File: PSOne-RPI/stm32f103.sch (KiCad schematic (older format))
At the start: 25 parts, among them J10 Controller-Port, J11 Controller-Port, J14 FAN1, J15 CN701, J16 CN702, SW1 PWR_BTN, SW2 CD_CLOSED, U5 ULN2003, U6 ULN2003, U7 STM32F103RBTx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

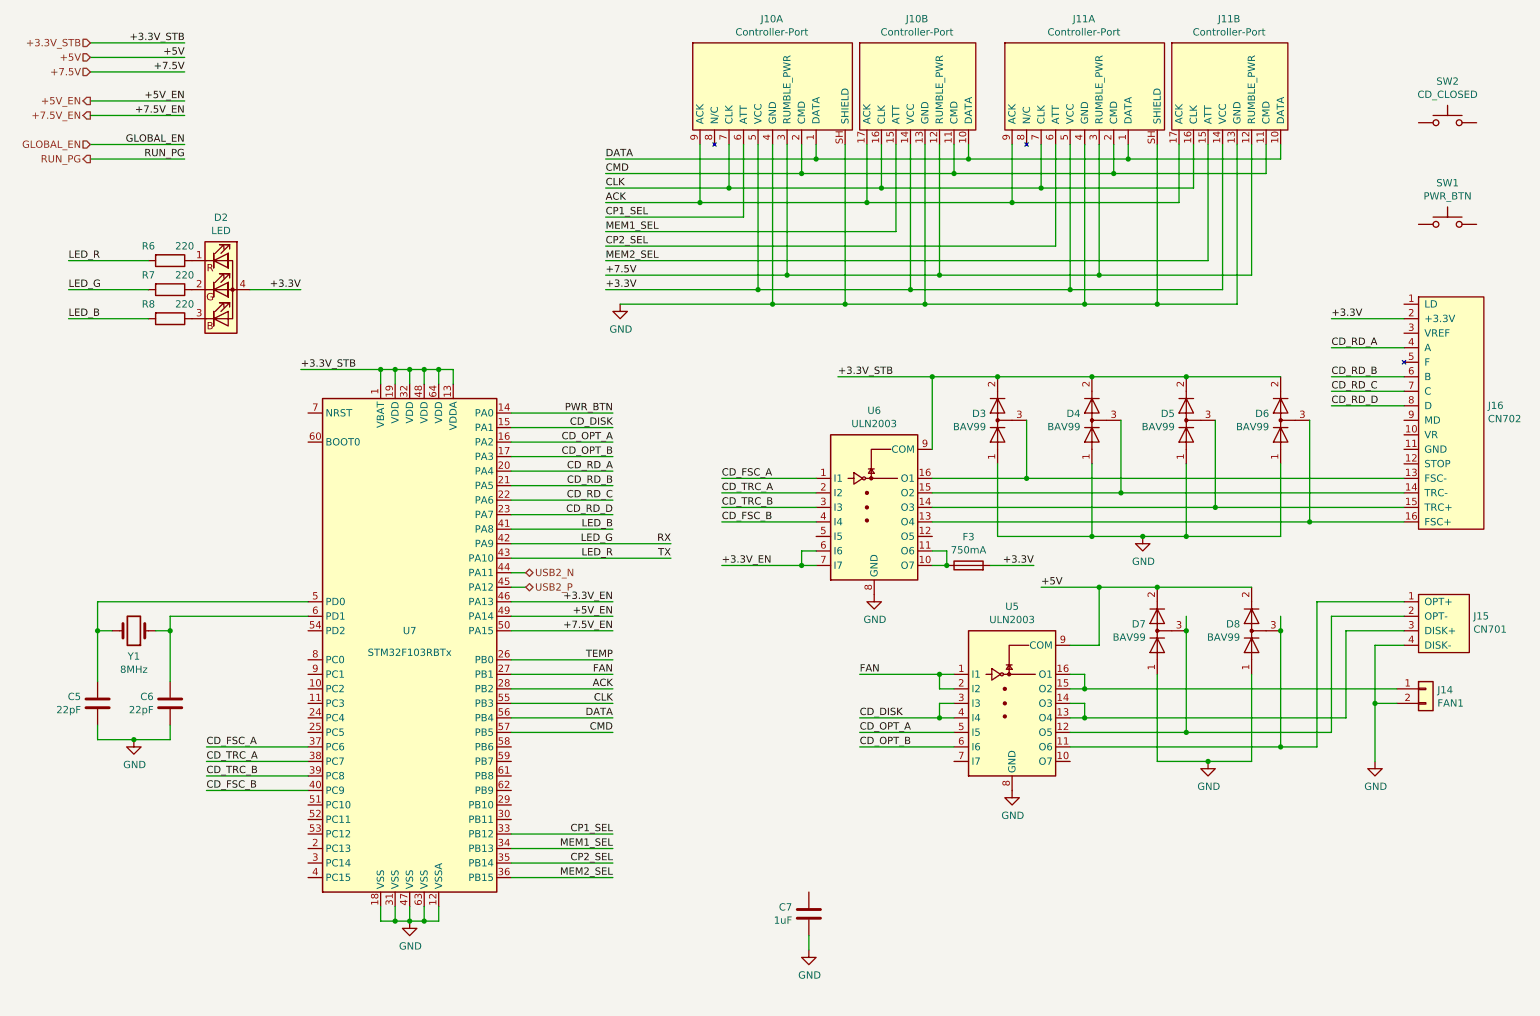
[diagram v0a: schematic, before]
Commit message: Cleaned schematic and moved CD interface to extra sheet
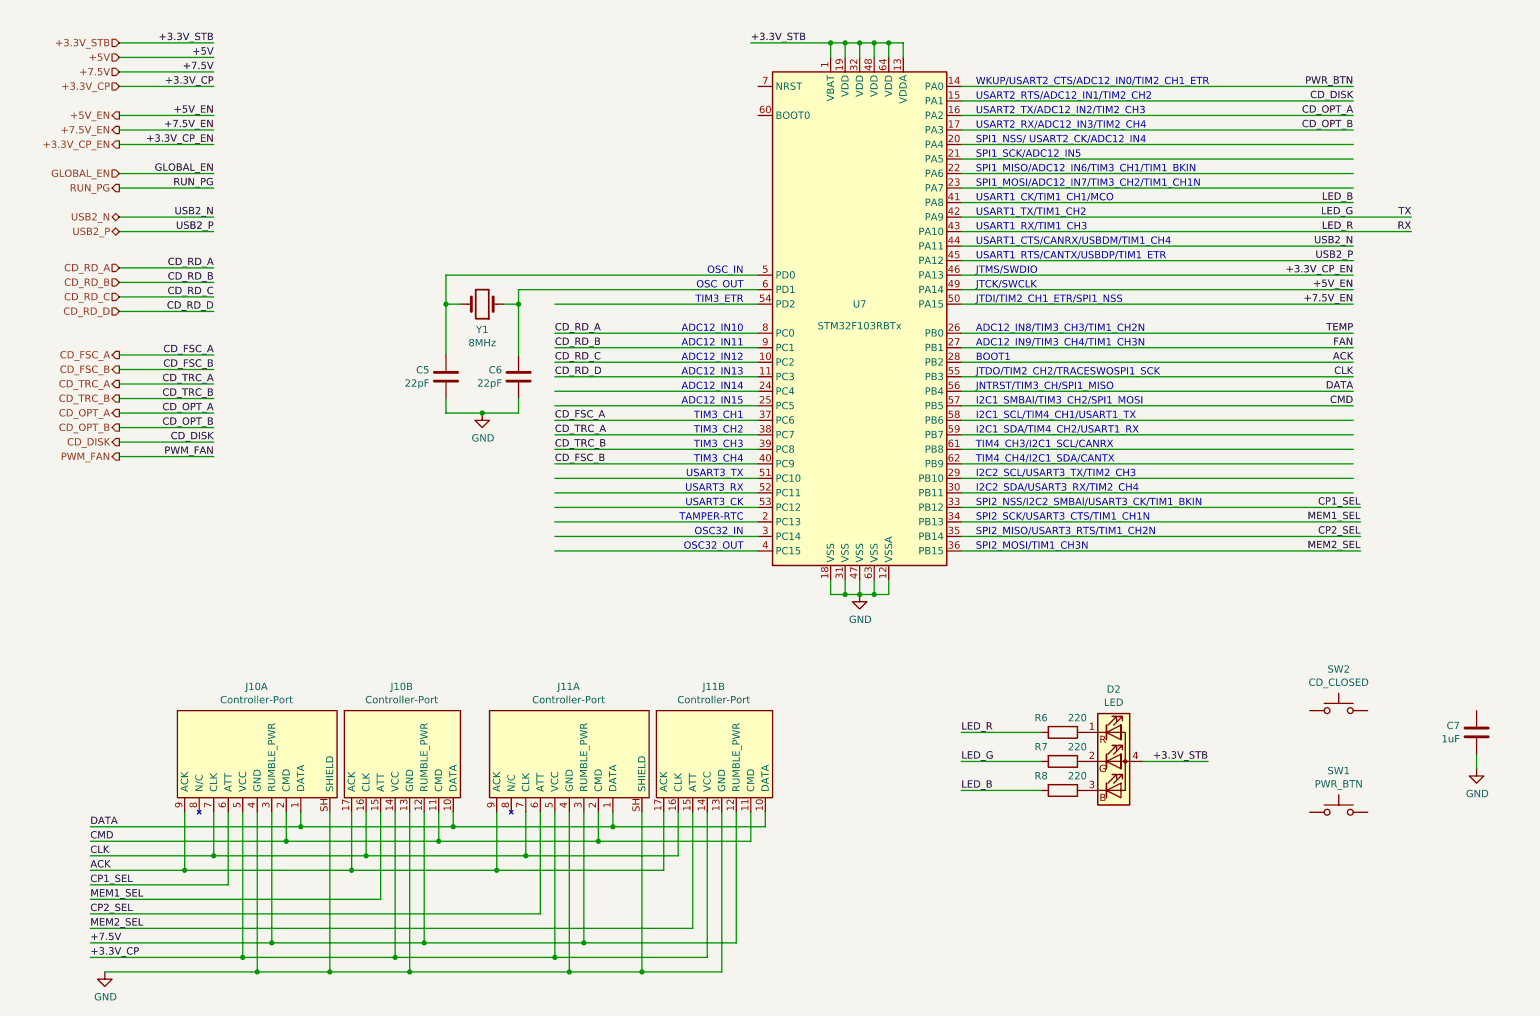
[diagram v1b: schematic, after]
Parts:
- removed D3, D4, D5, D6, D7, D8: BAV99, Package_TO_SOT_SMD:SOT-23, symbol Diode:BAV99
- removed F3: 750mA, Fuse:Fuse_1210_3225Metric, symbol Device:Fuse
- removed J14: FAN1, Connector_Hirose:Hirose_DF13-02P-1.25DSA_1x02_P1.25mm_Vertical, symbol Connector_Generic:Conn_01x02
- removed J15: CN701, Connector_Hirose:Hirose_DF13-04P-1.25DSA_1x04_P1.25mm_Vertical, symbol PSOne-RPI:CN701
- removed J16: CN702, PSOne-RPI:FFC-1x16-Vertical, symbol PSOne-RPI:CN702
- removed U5, U6: ULN2003, Package_SO:SOIC-16_3.9x9.9mm_P1.27mm, symbol Transistor_Array:ULN2003
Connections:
- net labels added: +3.3V_CP, +3.3V_CP_EN, PWM_FAN
- net labels removed: +3.3V, +3.3V_EN
- wire segments 231 -> 178
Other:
- note added: "ADC12_IN10"
- note added: "ADC12_IN11"
- note added: "ADC12_IN12"
- note added: "ADC12_IN13"
- note added: "ADC12_IN14"
- note added: "ADC12_IN15"
- note added: "ADC12_IN8/TIM3_CH3/TIM1_CH2N"
- note added: "ADC12_IN9/TIM3_CH4/TIM1_CH3N"
- note added: "BOOT1"
- note added: "I2C1_SCL/TIM4_CH1/USART1_TX"
- note added: "I2C1_SDA/TIM4_CH2/USART1_RX"
- note added: "I2C1_SMBAl/TIM3_CH2/SPI1_MOSI"
- note added: "I2C2_SCL/USART3_TX/TIM2_CH3"
- note added: "I2C2_SDA/USART3_RX/TIM2_CH4"
- note added: "JNTRST/TIM3_CH/SPI1_MISO"
- note added: "JTCK/SWCLK"
- note added: "JTDI/TIM2_CH1_ETR/SPI1_NSS"
- note added: "JTDO/TIM2_CH2/TRACESWOSPI1_SCK"
- note added: "JTMS/SWDIO"
- note added: "OSC32_IN"
- note added: "OSC32_OUT"
- note added: "OSC_IN"
- note added: "OSC_OUT"
- note added: "SPI1_MISO/ADC12_IN6/TIM3_CH1/TIM1_BKIN"
- note added: "SPI1_MOSI/ADC12_IN7/TIM3_CH2/TIM1_CH1N"
- note added: "SPI1_NSS/ USART2_CK/ADC12_IN4"
- note added: "SPI1_SCK/ADC12_IN5"
- note added: "SPI2_MISO/USART3_RTS/TIM1_CH2N"
- note added: "SPI2_MOSI/TIM1_CH3N"
- note added: "SPI2_NSS/I2C2_SMBAl/USART3_CK/TIM1_BKIN"
- note added: "SPI2_SCK/USART3_CTS/TIM1_CH1N"
- note added: "TAMPER-RTC"
- note added: "TIM3_CH1"
- note added: "TIM3_CH2"
- note added: "TIM3_CH3"
- note added: "TIM3_CH4"
- note added: "TIM3_ETR"
- note added: "TIM4_CH3/I2C1_SCL/CANRX"
- note added: "TIM4_CH4/I2C1_SDA/CANTX"
- note added: "USART1_CK/TIM1_CH1/MCO"
- note added: "USART1_CTS/CANRX/USBDM/TIM1_CH4"
- note added: "USART1_RTS/CANTX/USBDP/TIM1_ETR"
- note added: "USART1_RX/TIM1_CH3"
- note added: "USART1_TX/TIM1_CH2"
- note added: "USART2_RTS/ADC12_IN1/TIM2_CH2"
- note added: "USART2_RX/ADC12_IN3/TIM2_CH4"
- note added: "USART2_TX/ADC12_IN2/TIM2_CH3"
- note added: "USART3_CK"
- note added: "USART3_RX"
- note added: "USART3_TX"
- note added: "WKUP/USART2_CTS/ADC12_IN0/TIM2_CH1_ETR"
- moved on the sheet: C5, C6, C7, D2, J10A, J10B, J11A, J11B, R6, R7, R8, SW1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

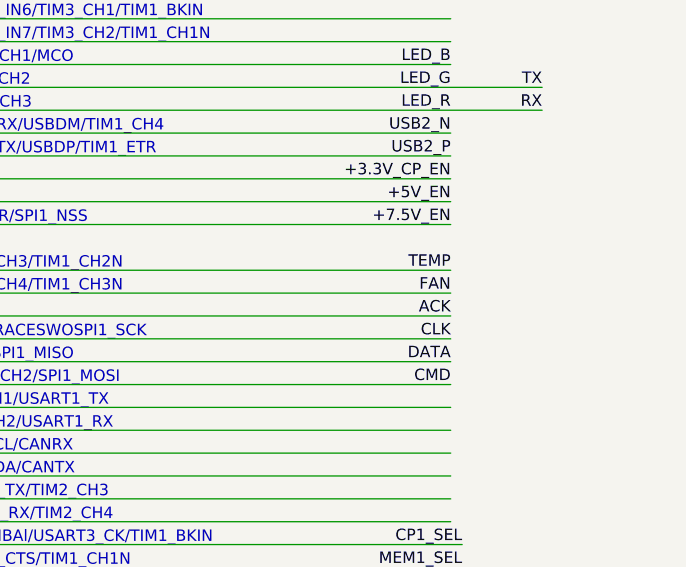
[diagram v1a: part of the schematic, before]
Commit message: Fixed naming FAN to PWM_FAN
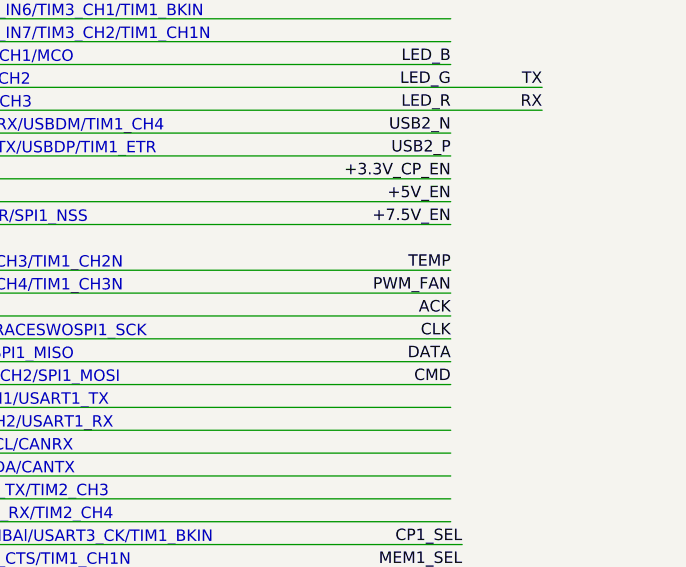
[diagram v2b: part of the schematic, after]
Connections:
- net labels removed: FAN
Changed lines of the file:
@@
 TEMP
 Text Label 9900 2950 2    50   ~ 0
-FAN
+PWM_FAN
 Text Label 9900 1450 2    50   ~ 0
 CD_OPT_B

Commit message: Finished CD drive interface circuit
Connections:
- net labels added: CD_LD, CD_MD, CD_STOP
- wire segments 178 -> 181
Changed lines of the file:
@@
 Text Label 2050 2700 2    50   ~ 0
 CD_RD_D
-Text HLabel 1400 3000 0    50   Output ~ 0
+Text HLabel 1400 2950 0    50   Output ~ 0
 CD_FSC_A
-Text HLabel 1400 3100 0    50   Output ~ 0
+Text HLabel 1400 3050 0    50   Output ~ 0
 CD_FSC_B
-Text HLabel 1400 3200 0    50   Output ~ 0
+Text HLabel 1400 3150 0    50   Output ~ 0
 CD_TRC_A
-Text HLabel 1400 3300 0    50   Output ~ 0
+Text HLabel 1400 3250 0    50   Output ~ 0
 CD_TRC_B
 Wire Wire Line
-	1400 3000 2050 3000
-Wire Wire Line
-	1400 3100 2050 3100
-Text Label 2050 3000 2    50   ~ 0
+	1400 2950 2050 2950
+Wire Wire Line
+	1400 3050 2050 3050
+Text Label 2050 2950 2    50   ~ 0
 CD_FSC_A
-Text Label 2050 3100 2    50   ~ 0
+Text Label 2050 3050 2    50   ~ 0
 CD_FSC_B
 Wire Wire Line
-	1400 3200 2050 3200
-Wire Wire Line
-	1400 3300 2050 3300
-Text Label 2050 3200 2    50   ~ 0
+	1400 3150 2050 3150
+Wire Wire Line
+	1400 3250 2050 3250
+Text Label 2050 3150 2    50   ~ 0
 CD_TRC_A
-Text Label 2050 3300 2    50   ~ 0
+Text Label 2050 3250 2    50   ~ 0
 CD_TRC_B
-Text HLabel 1400 3400 0    50   Output ~ 0
+Text HLabel 1400 3350 0    50   Output ~ 0
 CD_OPT_A
-Text HLabel 1400 3500 0    50   Output ~ 0
+Text HLabel 1400 3450 0    50   Output ~ 0
 CD_OPT_B
 Wire Wire Line
-	1400 3400 2050 3400
-Wire Wire Line
-	1400 3500 2050 3500
-Text Label 2050 3400 2    50   ~ 0
+	1400 3350 2050 3350
+Wire Wire Line
+	1400 3450 2050 3450
+Text Label 2050 3350 2    50   ~ 0
 CD_OPT_A
-Text Label 2050 3500 2    50   ~ 0
+Text Label 2050 3450 2    50   ~ 0
 CD_OPT_B
-Text HLabel 1400 3600 0    50   Output ~ 0
+Text HLabel 1400 3550 0    50   Output ~ 0
 CD_DISK
 Wire Wire Line
-	1400 3600 2050 3600
-Text Label 2050 3600 2    50   ~ 0
+	1400 3550 2050 3550
+Text Label 2050 3550 2    50   ~ 0
 CD_DISK
-Text HLabel 1400 3700 0    50   Output ~ 0
+Text HLabel 1400 4150 0    50   Output ~ 0
 PWM_FAN
 Wire Wire Line
-	1400 3700 2050 3700
-Text Label 2050 3700 2    50   ~ 0
+	1400 4150 2050 4150
+Text Label 2050 4150 2    50   ~ 0
 PWM_FAN
 Wire Wire Line
@@
 Wire Wire Line
 	8450 5800 8900 5800
+Text HLabel 1400 3750 0    50   Output ~ 0
+CD_MD
+Wire Wire Line
+	1400 3750 2050 3750
+Text Label 2050 3750 2    50   ~ 0
+CD_MD
+Text Label 9900 1750 2    50   ~ 0
+CD_MD
+Text HLabel 1400 3850 0    50   Input ~ 0
+CD_STOP
+Wire Wire Line
+	1400 3850 2050 3850
+Text Label 2050 3850 2    50   ~ 0
+CD_STOP
+Text HLabel 1400 3950 0    50   Output ~ 0
+CD_LD
+Wire Wire Line
+	1400 3950 2050 3950
+Text Label 2050 3950 2    50   ~ 0
+CD_LD
+Text Label 9900 1550 2    50   ~ 0
+CD_STOP
+Text Label 9900 1650 2    50   ~ 0
+CD_LD
 $EndSCHEMATC

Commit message: Updated internal power supply
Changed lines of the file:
@@
 Text Label 9900 1950 2    50   ~ 0
 LED_B
+Text Label 4400 3550 0    50   ~ 0
+CD_TRC_B
 Text Label 4400 3650 0    50   ~ 0
-CD_TRC_B
-Text Label 4400 3550 0    50   ~ 0
 CD_TRC_A
+Text Label 4400 3750 0    50   ~ 0
+CD_FSC_A
 Text Label 4400 3450 0    50   ~ 0
-CD_FSC_A
-Text Label 4400 3750 0    50   ~ 0
 CD_FSC_B
 Text Label 9900 2850 2    50   ~ 0
@@
 Text Label 5750 850  0    50   ~ 0
 +3.3V_STB
-Text Label 9900 3050 2    50   ~ 0
+Text Label 9900 3450 2    50   ~ 0
 ACK
 Text Label 9900 3150 2    50   ~ 0
@@
 Text Label 9900 3250 2    50   ~ 0
 DATA
-Text Label 9950 4350 2    50   ~ 0
+Text Label 9900 4250 2    50   ~ 0
 MEM2_SEL
-Text Label 9950 4150 2    50   ~ 0
+Text Label 9900 4050 2    50   ~ 0
 MEM1_SEL
-Text Label 9950 4050 2    50   ~ 0
+Text Label 9900 4150 2    50   ~ 0
 CP1_SEL
-Text Label 9950 4250 2    50   ~ 0
+Text Label 9900 4350 2    50   ~ 0
 CP2_SEL
 Text HLabel 1400 850  0    50   Input ~ 0
@@
 	7200 1350 9900 1350
 Wire Wire Line
-	7200 4250 9950 4250
-Wire Wire Line
-	7200 4350 9950 4350
-Wire Wire Line
 	7200 3850 9900 3850
 Wire Wire Line
 	7200 3950 9900 3950
-Wire Wire Line
-	7200 4050 9950 4050
-Wire Wire Line
-	7200 4150 9950 4150
 Text Notes 7300 1250 0    50   ~ 0
 USART2_RTS/ADC12_IN1/TIM2_CH2
@@
 Text Label 9900 1650 2    50   ~ 0
 CD_LD
+Wire Wire Line
+	7200 4050 9900 4050
+Wire Wire Line
+	7200 4150 9900 4150
+Wire Wire Line
+	7200 4250 9900 4250
+Wire Wire Line
+	7200 4350 9900 4350
 $EndSCHEMATC
